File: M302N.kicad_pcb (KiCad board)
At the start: 2 copper layers, 100.1 x 56 mm, 36 parts, among them J1 DC12V, J10 ADC_IN, J11 RJ45, J12 DC12V FAN, J13 Conn_01x05_Socket, J14 Conn_01x05_Socket, J18 Conn_01x04_Socket, J19 Conn_01x04_Socket, J2 UART, J3 extend I/O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

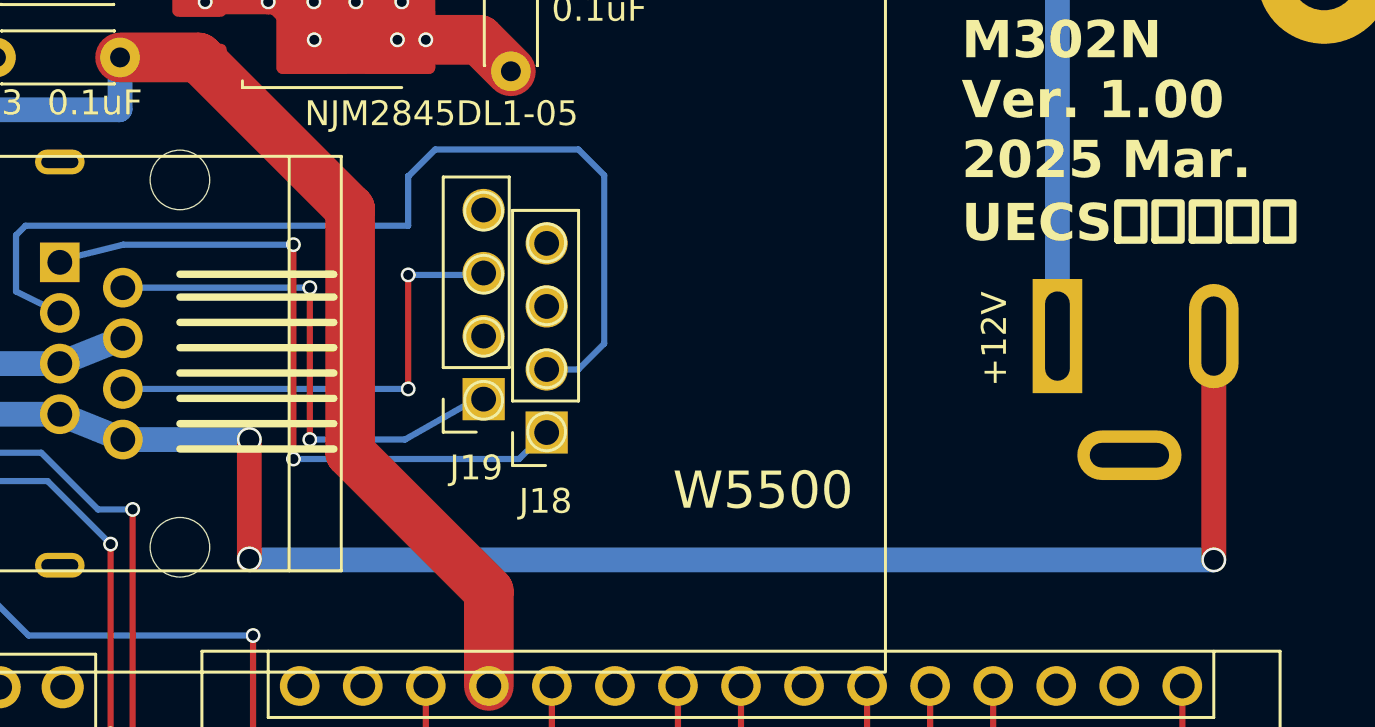
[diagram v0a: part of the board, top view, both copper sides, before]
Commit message: 回路図上の変更は完了。PCB部品の選定に入る所。
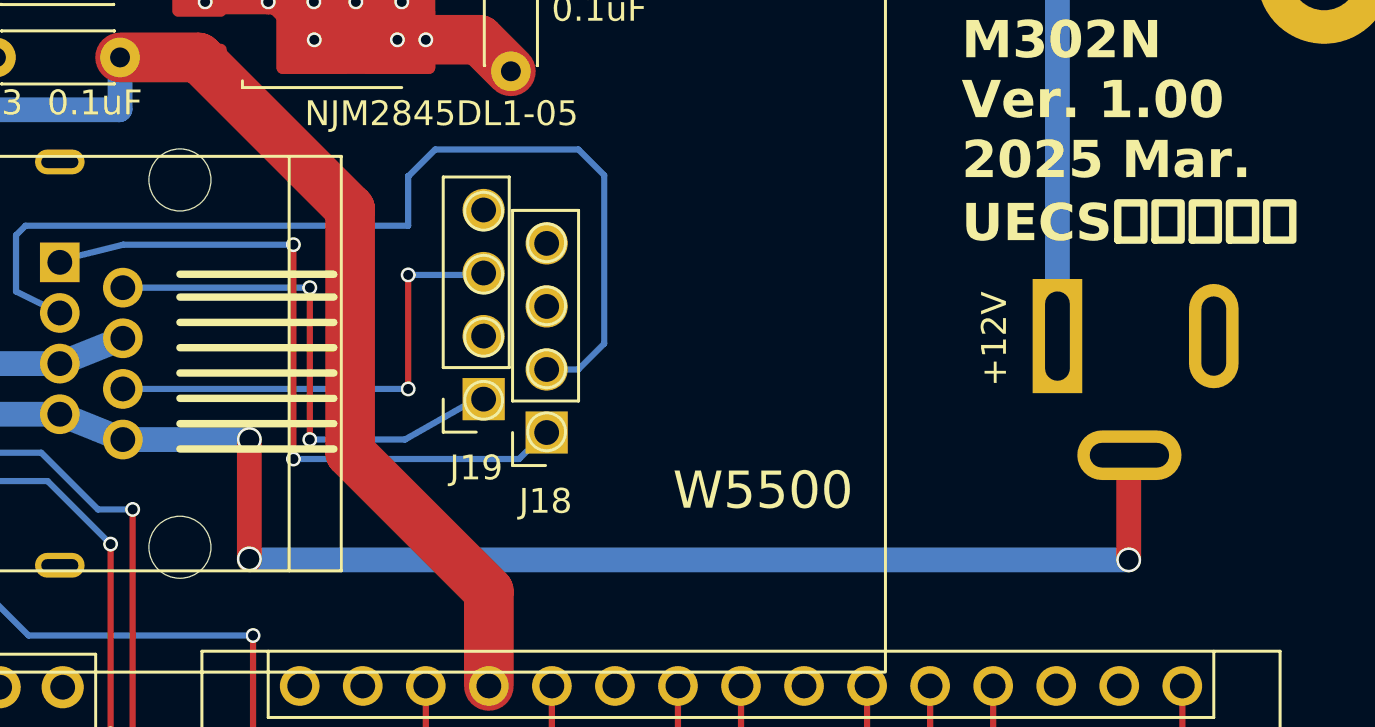
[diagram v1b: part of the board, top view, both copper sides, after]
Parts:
- J1: footprint Connector_BarrelJack:BarrelJack_GCT_DCJ200-10-A_Horizontal -> Connector_BarrelJack:MJ-179PH
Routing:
- net Net-(J1-Pad2): track 76.1 -> 67.9 mm
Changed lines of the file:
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@@
 		(pad "" np_thru_hole circle
 			(at -7.4 0 90)
-			(size 2.4 2.4)
-			(drill 2.4)
-			(layers "*.Cu" "*.Mask" "In1.Cu" "In2.Cu" "In3.Cu" "In4.Cu" "In5.Cu" "In6.Cu"
-				"In7.Cu" "In8.Cu" "In9.Cu" "In10.Cu" "In11.Cu" "In12.Cu" "In13.Cu" "In14.Cu"
-				"In15.Cu" "In16.Cu" "In17.Cu" "In18.Cu" "In19.Cu" "In20.Cu" "In21.Cu"
-				"In22.Cu" "In23.Cu" "In24.Cu" "In25.Cu" "In26.Cu" "In27.Cu" "In28.Cu"
-				"In29.Cu" "In30.Cu"
-			)
+			(size 2.5 2.5)
+			(drill 2.5)
+			(layers "*.Cu" "*.Mask")
 		)
 		(pad "" np_thru_hole circle
 			(at 7.4 0 90)
-			(size 2.4 2.4)
-			(drill 2.4)
-			(layers "*.Cu" "*.Mask" "In1.Cu" "In2.Cu" "In3.Cu" "In4.Cu" "In5.Cu" "In6.Cu"
-				"In7.Cu" "In8.Cu" "In9.Cu" "In10.Cu" "In11.Cu" "In12.Cu" "In13.Cu" "In14.Cu"
-				"In15.Cu" "In16.Cu" "In17.Cu" "In18.Cu" "In19.Cu" "In20.Cu" "In21.Cu"
-				"In22.Cu" "In23.Cu" "In24.Cu" "In25.Cu" "In26.Cu" "In27.Cu" "In28.Cu"
-				"In29.Cu" "In30.Cu"
-			)
+			(size 2.5 2.5)
+			(drill 2.5)
+			(layers "*.Cu" "*.Mask")
 		)
 		(pad "" thru_hole oval
@@
 		)
 	)
-	(footprint "Connector_BarrelJack:BarrelJack_GCT_DCJ200-10-A_Horizontal"
+	(footprint "Connector_BarrelJack:MJ-179PH"
 		(layer "B.Cu")
 		(at 156.26 77.3436 -90)
@@
 		(tags "connector barrel jack")
 		(property "Reference" "J1"
-			(at 6.3494 -11.761 0)
+			(at 6.3494 -11.761 180)
 			(layer "B.SilkS")
 			(effects
@@
 		)
 		(pad "2" thru_hole oval
-			(at 0 -6.3 270)
-			(size 4.2 2)
-			(drill oval 3.2 1)
+			(at 4.8 -2.9 270)
+			(size 2 4.2)
+			(drill oval 1 3.2)
 			(layers "*.Cu" "*.Mask" "In1.Cu" "In2.Cu" "In3.Cu" "In4.Cu" "In5.Cu" "In6.Cu"
 				"In7.Cu" "In8.Cu" "In9.Cu" "In10.Cu" "In11.Cu" "In12.Cu" "In13.Cu" "In14.Cu"
@@
 		)
 		(pad "3" thru_hole oval
-			(at 4.8 -2.9 270)
-			(size 2 4.2)
-			(drill oval 1 3.2)
+			(at 0 -6.3 270)
+			(size 4.2 2)
+			(drill oval 3.2 1)
 			(layers "*.Cu" "*.Mask" "In1.Cu" "In2.Cu" "In3.Cu" "In4.Cu" "In5.Cu" "In6.Cu"
 				"In7.Cu" "In8.Cu" "In9.Cu" "In10.Cu" "In11.Cu" "In12.Cu" "In13.Cu" "In14.Cu"
@@
 	)
 	(segment
-		(start 162.56 86.36)
-		(end 162.56 77.3436)
+		(start 159.131 82.1726)
+		(end 159.16 82.1436)
+		(width 1)
+		(layer "F.Cu")
+		(net 27)
+	)
+	(segment
+		(start 159.131 86.36)
+		(end 159.131 82.1726)
 		(width 1)
 		(layer "F.Cu")
@@
 	)
 	(via
-		(at 162.56 86.36)
+		(at 159.131 86.36)
 		(size 1)
 		(drill 0.8)
@@
 	)
 	(segment
-		(start 118.604 81.512)
-		(end 123.7 81.512)
-		(width 1)
-		(layer "B.Cu")
-		(net 27)
-	)
-	(segment
-		(start 116.064 80.492)
-		(end 118.604 81.512)
+		(start 159.131 86.36)
+		(end 123.7 86.36)
 		(width 1)
 		(layer "B.Cu")
@@
 	)
 	(segment
-		(start 162.5092 86.36)
-		(end 162.56 86.36)
+		(start 118.604 81.512)
+		(end 123.7 81.512)
 		(width 1)
 		(layer "B.Cu")
@@
 	)
 	(segment
-		(start 123.7 86.36)
-		(end 162.5092 86.36)
+		(start 116.064 80.492)
+		(end 118.604 81.512)
 		(width 1)
 		(layer "B.Cu")

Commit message: v2.00 PCB変更とスイッチングレギュレータ採用検討
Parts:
- removed J10, J8, J9: ADC_IN, Connector_JST:JST_XH_B3B-XH-A_1x03_P2.50mm_Vertical
- removed SW1: SW_Reed, HOLLY:REED_SW
- added D4: 1S4, Resistor_THT:R_Axial_DIN0204_L3.6mm_D1.6mm_P5.08mm_Horizontal, F.Cu at (145.6, 60.7)
- added J6: ADC_IN, Connector_JST:JST_XH_B3B-XH-A_1x03_P2.50mm_Vertical, F.Cu at (148.9, 47.9)
- added J7: RESET, Connector_JST:JST_XH_S2B-XH-A_1x02_P2.50mm_Horizontal, F.Cu at (139.5, 47.9)
- J1: footprint Connector_BarrelJack:MJ-179PH -> Connector_BarrelJack:BarrelJack_GCT_DCJ200-10-A_Horizontal
- J2: footprint Connector_PinHeader_2.54mm:PinHeader_1x03_P2.54mm_Vertical -> Connector_JST:JST_XH_S4B-XH-A_1x04_P2.50mm_Horizontal
- moved J2 0.06 mm to (159.1, 95.8), turned to -90 degrees
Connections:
- A1 pad 1: Net-(A1-D1/TX) -> unconnected-(A1-D1/TX-Pad1)
- A1 pad 11: Net-(A1-D8) -> /RX
- A1 pad 12: Net-(A1-D9) -> /TX
- A1 pad 2: Net-(A1-D0/RX) -> unconnected-(A1-D0/RX-Pad2)
- A1 pad 20: Net-(A1-A1) -> unconnected-(A1-A1-Pad20)
- A1 pad 21: Net-(A1-A2) -> unconnected-(A1-A2-Pad21)
- A1 pad 5: unconnected-(A1-D2-Pad5) -> Net-(A1-D2)
- A1 pad 6: /*D3 -> Net-(A1-D3)
- D2 pad 2: /*D3 -> Net-(A1-A0)
- J1 pad 1: /+12V -> Net-(D4-A)
- J2 pad 2: Net-(A1-D0/RX) -> /RX
- J2 pad 3: Net-(A1-D1/TX) -> /TX
- J3 pad 1: Net-(A1-D9) -> Net-(A1-D2)
- J3 pad 11: Net-(A1-D4) -> Net-(A1-D7)
- J3 pad 3: Net-(A1-D8) -> Net-(A1-D3)
- J3 pad 5: Net-(A1-D7) -> Net-(A1-D4)
- J3 pad 7: Net-(A1-D6) -> Net-(A1-D5)
- J3 pad 9: Net-(A1-D5) -> Net-(A1-D6)
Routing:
- net Net-(A1-A2): track 83.9 -> 0.00 mm, vias 5 -> 0
- net Net-(A1-A1): track 77.6 -> 0.00 mm, vias 5 -> 0
- net /*D3: track 76.8 -> 0.00 mm, vias 3 -> 0
- net Net-(A1-D9): track 66.0 -> 0.00 mm, vias 3 -> 0
- net Net-(A1-D8): track 59.9 -> 0.00 mm, vias 3 -> 0
- net +5V: track 162.0 -> 213.3 mm, vias 3 -> 7
- net Net-(A1-D2): track 0.00 -> 48.2 mm, vias 0 -> 3
- net Net-(A1-D3): track 0.00 -> 47.2 mm, vias 0 -> 3
- net Net-(A1-D0/RX): track 39.2 -> 0.00 mm, vias 1 -> 0
- net Net-(A1-D1/TX): track 39.1 -> 0.00 mm, vias 1 -> 0
- net /+12V: track 90.9 -> 64.5 mm
- net Net-(A1-A0): track 65.0 -> 90.2 mm
- net Net-(D4-A): track 0.00 -> 22.2 mm, vias 0 -> 1
- net /RX: track 0.00 -> 15.8 mm, vias 0 -> 1
- net /TX: track 0.00 -> 13.1 mm, vias 0 -> 1
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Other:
- board text added: "M302N Ver. 2.00 2025 June"
- board text removed: "A0"
- board text removed: "A1"
- board text removed: "A2"
- board text removed: "M302N Ver. 1.00 2025 Mar."

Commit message: 大胆な変更
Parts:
- removed C3, C6: 0.1uF, Capacitor_THT:C_Disc_D4.3mm_W1.9mm_P5.00mm
- J7: footprint Connector_JST:JST_XH_S2B-XH-A_1x02_P2.50mm_Horizontal -> Connector_JST:JST_XH_B2B-XH-A_1x02_P2.50mm_Vertical
- U2: value NJM2845DL1-05 -> BP5293-50; footprint Package_TO_SOT_SMD:TO-252-3_TabPin2 -> footprints:SIP03_BP5293_17X7P2_ROM
- moved J6 77.0 mm to (96.5, 104.4), turned to 90 degrees
- moved J7 64.3 mm to (109.7, 104.8)
- moved U2 27.8 mm to (100.1, 71.8)
- moved C5 26.6 mm to (107.7, 64.1), turned to 180 degrees
- moved C2 23.5 mm to (95.0, 64.1), turned to 0 degrees
- moved C1 17.6 mm to (91.5, 71.2), turned to -90 degrees
- moved C4 15.7 mm to (82.5, 79.2), turned to 0 degrees
- moved F1 12.6 mm to (90.7, 83.7), turned to 90 degrees
- moved D1 9.41 mm to (96.4, 75.8)
- moved D4 7.24 mm to (140.4, 65.8), turned to 0 degrees
- moved R2 2.80 mm to (103.5, 99.8)
- moved FL1 2.78 mm to (85.4, 74.2)
- moved R1 2.29 mm to (80.7, 103.1)
- moved J2 0.46 mm to (159.1, 95.3)
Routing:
- net +5V: track 213.3 -> 113.1 mm
- net /+12V: track 64.5 -> 0.00 mm, vias 1 -> 0
- net Net-(U2-VIN): track 56.9 -> 0.00 mm, vias 4 -> 0
- net Net-(D3-K): track 46.6 -> 11.3 mm, vias 1 -> 0
- net /A4/SDA: track 124.7 -> 91.0 mm
- net GND: track 18.8 -> 8.43 mm, vias 9 -> 1
- net Net-(A1-A0): track 90.2 -> 81.4 mm
- net Net-(D1-A): track 17.4 -> 12.0 mm
- net /TX: track 13.1 -> 11.8 mm
- net Net-(A1-D13): track 86.5 -> 87.1 mm

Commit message: v2.00 ほぼ完成？
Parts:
- moved D4 26.9 mm to (113.5, 67.0)
- moved C2 5.15 mm to (100.1, 64.1), turned to 180 degrees
- moved C5 5.08 mm to (102.6, 64.1), turned to 0 degrees
- moved C1 1.95 mm to (90.9, 69.3)
- moved F1 0.42 mm to (90.7, 84.1)
- moved R2 0.39 mm to (103.5, 99.4)
- moved FL1 0.36 mm to (85.0, 74.2)
- moved U2 0.05 mm to (100.1, 71.8)
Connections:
- J11 pad : (no net) -> GND
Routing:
- net +5V: track 113.1 -> 266.3 mm
- net Net-(A1-A3): track 0.00 -> 59.1 mm, vias 0 -> 1
- net Net-(U2-VIN): track 0.00 -> 36.4 mm, vias 0 -> 1
- net /A4/SDA: track 91.0 -> 126.9 mm
- net /+12V: track 0.00 -> 28.3 mm
- net Net-(D4-A): track 22.2 -> 47.9 mm, vias 1 -> 2
- net Net-(D3-K): track 11.3 -> 35.6 mm, vias 0 -> 1
- net Net-(A1-A0): track 81.4 -> 105.0 mm, vias 1 -> 5
- net GND: track 8.43 -> 17.5 mm, vias 1 -> 2
- net /~{RESET}: track 86.4 -> 79.8 mm, vias 4 -> 3
- net Net-(D1-A): track 12.0 -> 18.4 mm
